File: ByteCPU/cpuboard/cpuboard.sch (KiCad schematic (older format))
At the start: 4 parts, among them J1 Conn_01x06, J2 Conn_01x20, J3 Conn_01x08

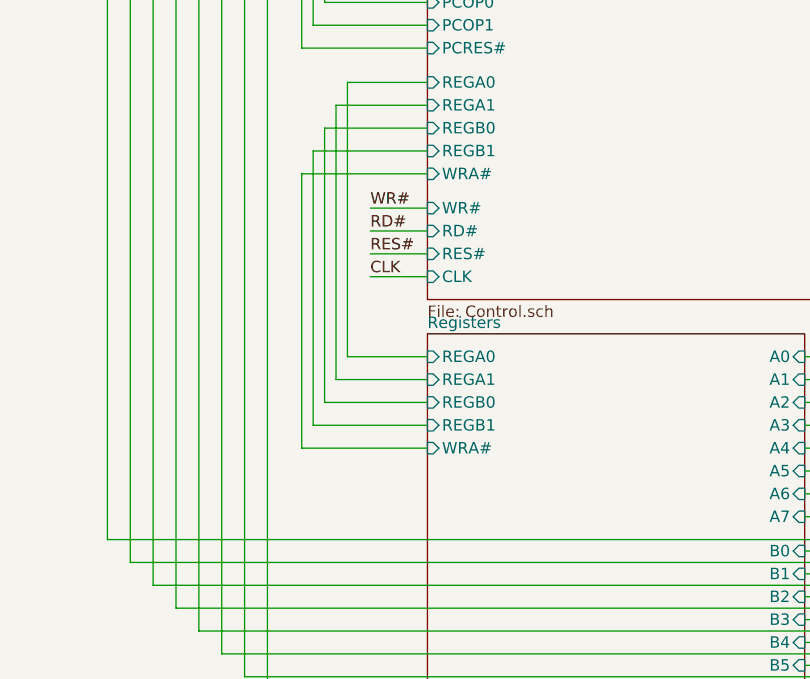
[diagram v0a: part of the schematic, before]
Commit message: Fix mistake in SELPC signal generation. More docu.
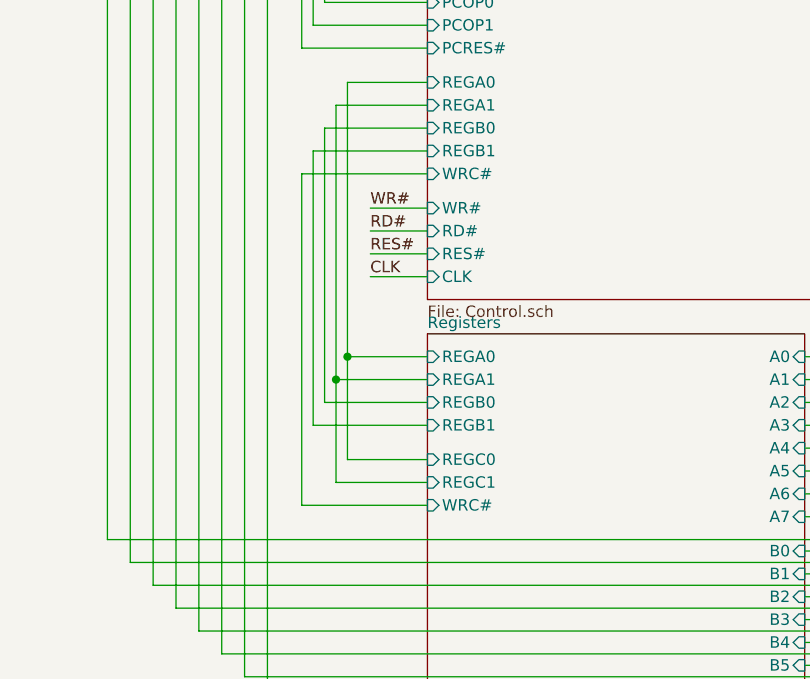
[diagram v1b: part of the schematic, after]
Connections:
- wire segments 221 -> 225
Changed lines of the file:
@@
 F0 "Registers" 50
 F1 "registers.sch" 50
-F2 "WRA#" I L 2000 5500 50
-F3 "CLK" I L 2000 7500 50
-F4 "C0" I R 3650 6800 50
-F5 "C1" I R 3650 6900 50
-F6 "C2" I R 3650 7000 50
-F7 "C3" I R 3650 7100 50
-F8 "C4" I R 3650 7200 50
-F9 "C5" I R 3650 7300 50
-F10 "C6" I R 3650 7400 50
-F11 "C7" I R 3650 7500 50
-F12 "REGB0" I L 2000 5300 50
-F13 "REGB1" I L 2000 5400 50
-F14 "REGA0" I L 2000 5100 50
-F15 "REGA1" I L 2000 5200 50
-F16 "A0" I R 3650 5100 50
-F17 "A1" I R 3650 5200 50
-F18 "A2" I R 3650 5300 50
-F19 "A3" I R 3650 5400 50
-F20 "A4" I R 3650 5500 50
-F21 "A5" I R 3650 5600 50
-F22 "A6" I R 3650 5700 50
-F23 "A7" I R 3650 5800 50
-F24 "B0" I R 3650 5950 50
-F25 "B1" I R 3650 6050 50
-F26 "B2" I R 3650 6150 50
-F27 "B3" I R 3650 6250 50
-F28 "B4" I R 3650 6350 50
-F29 "B5" I R 3650 6450 50
-F30 "B6" I R 3650 6550 50
-F31 "B7" I R 3650 6650 50
+F2 "CLK" I L 2000 7500 50
+F3 "C0" I R 3650 6800 50
+F4 "C1" I R 3650 6900 50
+F5 "C2" I R 3650 7000 50
+F6 "C3" I R 3650 7100 50
+F7 "C4" I R 3650 7200 50
+F8 "C5" I R 3650 7300 50
+F9 "C6" I R 3650 7400 50
+F10 "C7" I R 3650 7500 50
+F11 "REGB0" I L 2000 5300 50
+F12 "REGB1" I L 2000 5400 50
+F13 "REGA0" I L 2000 5100 50
+F14 "REGA1" I L 2000 5200 50
+F15 "A0" I R 3650 5100 50
+F16 "A1" I R 3650 5200 50
+F17 "A2" I R 3650 5300 50
+F18 "A3" I R 3650 5400 50
+F19 "A4" I R 3650 5500 50
+F20 "A5" I R 3650 5600 50
+F21 "A6" I R 3650 5700 50
+F22 "A7" I R 3650 5800 50
+F23 "B0" I R 3650 5950 50
+F24 "B1" I R 3650 6050 50
+F25 "B2" I R 3650 6150 50
+F26 "B3" I R 3650 6250 50
+F27 "B4" I R 3650 6350 50
+F28 "B5" I R 3650 6450 50
+F29 "B6" I R 3650 6550 50
+F30 "B7" I R 3650 6650 50
+F31 "WRC#" I L 2000 5750 50
+F32 "REGC0" I L 2000 5550 50
+F33 "REGC1" I L 2000 5650 50
 $EndSheet
 $Sheet
@@
 F19 "WRDP#" I L 2000 3450 50
 F20 "SELALU#" I R 5800 4250 50
-F21 "WRA#" I L 2000 4300 50
-F22 "ISTRUE" I R 5800 4350 50
-F23 "REGA0" I L 2000 3900 50
-F24 "REGA1" I L 2000 4000 50
-F25 "REGB0" I L 2000 4100 50
-F26 "REGB1" I L 2000 4200 50
-F27 "OP1" I R 5800 4500 50
-F28 "OP2" I R 5800 4600 50
-F29 "OP3" I R 5800 4700 50
+F21 "ISTRUE" I R 5800 4350 50
+F22 "REGA0" I L 2000 3900 50
+F23 "REGA1" I L 2000 4000 50
+F24 "REGB0" I L 2000 4100 50
+F25 "REGB1" I L 2000 4200 50
+F26 "OP1" I R 5800 4500 50
+F27 "OP2" I R 5800 4600 50
+F28 "OP3" I R 5800 4700 50
+F29 "WRC#" I L 2000 4300 50
 $EndSheet
 Text Label 9150 6350 3    50   ~ 0
@@
 	1650 3900 1650 5100
 Wire Wire Line
-	1650 5100 2000 5100
-Wire Wire Line
 	2000 5200 1600 5200
 Wire Wire Line
@@
 Wire Wire Line
 	2000 4300 1450 4300
-Wire Wire Line
-	1450 4300 1450 5500
-Wire Wire Line
-	1450 5500 2000 5500
 Text Label 1750 4750 0    50   ~ 0
 CLK
@@
 Text Notes 10250 5200 0    50   ~ 0
 Add a 100nF ceramic \ncapacitor to every IC.
+Wire Wire Line
+	1450 5750 2000 5750
+Wire Wire Line
+	1450 4300 1450 5750
+Wire Wire Line
+	1650 5100 2000 5100
+Wire Wire Line
+	1650 5100 1650 5550
+Wire Wire Line
+	1650 5550 2000 5550
+Connection ~ 1650 5100
+Wire Wire Line
+	1600 5200 1600 5650
+Wire Wire Line
+	1600 5650 2000 5650
+Connection ~ 1600 5200
 $EndSCHEMATC

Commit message: Modifications to fit the wiring to the physical layout of the 7400 logic. Bugfix: RD line was active during JMP instruction.
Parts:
- removed J2: Conn_01x20, symbol Connector_Generic:Conn_01x20
- added J2: Conn_01x18, symbol Connector_Generic:Conn_01x18
- added U1: 7400, symbol 74xx:7400
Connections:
- wire segments 225 -> 246
- no-connect marks 0 -> 1

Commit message: Rework control logic to allow and additional IO instruction
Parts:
- removed J1: Conn_01x06, symbol Connector_Generic:Conn_01x06
- removed J2: Conn_01x18, symbol Connector_Generic:Conn_01x18
- removed unit 3 of U1
- removed unit 4 of U1
- added J1: Conn_01x07, symbol Connector_Generic:Conn_01x07
- added J2: Conn_01x17, symbol Connector_Generic:Conn_01x17
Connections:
- net labels added: IO#
- wire segments 246 -> 237
- no-connect marks 1 -> 0
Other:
- moved on the sheet: U1B
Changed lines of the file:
@@
 F40 "COUNT" I L 2000 2750 50
-$EndSheet
-$Sheet
-S 2000 3200 3800 1650
-U 6088908D
-F0 "Control" 50
-F1 "Control.sch" 50
-F2 "D0" I R 5800 3300 50
-F3 "D1" I R 5800 3400 50
-F4 "D2" I R 5800 3500 50
-F5 "D3" I R 5800 3600 50
-F6 "D4" I R 5800 3700 50
-F7 "D5" I R 5800 3800 50
-F8 "D6" I R 5800 3900 50
-F9 "D7" I R 5800 4000 50
-F10 "CLK" I L 2000 4750 50
-F11 "RES#" I L 2000 4650 50
-F12 "WR#" I L 2000 4450 50
-F13 "RD#" I L 2000 4550 50
-F14 "PCRES#" I L 2000 3800 50
-F15 "SELPC" I L 2000 3300 50
-F16 "OEA#" I R 5800 4150 50
-F17 "WRDP#" I L 2000 3400 50
-F18 "SELALU#" I R 5800 4250 50
-F19 "ISTRUE" I R 5800 4350 50
-F20 "REGA0" I L 2000 3900 50
-F21 "REGA1" I L 2000 4000 50
-F22 "REGB0" I L 2000 4100 50
-F23 "REGB1" I L 2000 4200 50
-F24 "OP1" I R 5800 4500 50
-F25 "OP2" I R 5800 4600 50
-F26 "OP3" I R 5800 4700 50
-F27 "WRC#" I L 2000 4300 50
-F28 "COUNT" I L 2000 3700 50
-F29 "LOADLOW#" I L 2000 3600 50
-F30 "LOADHIGH#" I L 2000 3500 50
 $EndSheet
 Text Label 9650 6350 3    50   ~ 0
@@
 	3800 6650 4200 6650
 $Comp
-L Connector_Generic:Conn_01x06 J1
-U 1 1 60D740B8
-P 950 650
-F 0 "J1" V 916 930 50  0000 L CNN
-F 1 "Conn_01x06" V 1050 400 50  0000 L CNN
-F 2 "" H 950 650 50  0001 C CNN
-F 3 "~" H 950 650 50  0001 C CNN
-	1    950  650
-	0    1    -1   0
-$EndComp
-$Comp
 L power:GND #PWR0145
 U 1 1 60D7414A
@@
 Wire Wire Line
 	2000 4300 1450 4300
-Text Label 1750 4750 0    50   ~ 0
+Text Label 1750 4800 0    50   ~ 0
 CLK
-Text Label 1750 4650 0    50   ~ 0
+Text Label 1750 4700 0    50   ~ 0
 RES#
-Text Label 1750 4550 0    50   ~ 0
+Text Label 1750 4600 0    50   ~ 0
 RD#
-Text Label 1750 4450 0    50   ~ 0
+Text Label 1750 4500 0    50   ~ 0
 WR#
 Wire Wire Line
-	1750 4450 2000 4450
-Wire Wire Line
-	1750 4550 2000 4550
-Wire Wire Line
-	1750 4650 2000 4650
-Wire Wire Line
-	1750 4750 2000 4750
+	1750 4500 2000 4500
+Wire Wire Line
+	1750 4600 2000 4600
+Wire Wire Line
+	1750 4700 2000 4700
+Wire Wire Line
+	1750 4800 2000 4800
 Wire Wire Line
 	5800 4150 6100 4150
@@
 P 1150 1300
 F 0 "U1" H 1350 1550 50  0000 C CNN
-F 1 "7400" H 1350 1450 50  0000 C CNN
+F 1 "7400" H 1400 1450 50  0000 C CNN
 F 2 "" H 1150 1300 50  0001 C CNN
 F 3 "http://www.ti.com/lit/gpn/sn7400" H 1150 1300 50  0001 C CNN
@@
 L 74xx:7400 U1
 U 2 1 5FAC56A9
-P 6500 850
-F 0 "U1" H 6650 1150 50  0000 C CNN
-F 1 "7400" H 6650 1050 50  0000 C CNN
-F 2 "" H 6500 850 50  0001 C CNN
-F 3 "http://www.ti.com/lit/gpn/sn7400" H 6500 850 50  0001 C CNN
-	2    6500 850
-	1    0    0    -1
-$EndComp
-$Comp
-L 74xx:7400 U1
-U 3 1 5FAC56F1
-P 10650 2550
-F 0 "U1" H 10650 2875 50  0000 C CNN
-F 1 "7400" H 10650 2784 50  0000 C CNN
-F 2 "" H 10650 2550 50  0001 C CNN
-F 3 "http://www.ti.com/lit/gpn/sn7400" H 10650 2550 50  0001 C CNN
-	3    10650 2550
-	1    0    0    -1
-$EndComp
-$Comp
-L 74xx:7400 U1
-U 4 1 5FAC573E
-P 6500 1250
-F 0 "U1" H 6700 1500 50  0000 C CNN
-F 1 "7400" H 6700 1400 50  0000 C CNN
-F 2 "" H 6500 1250 50  0001 C CNN
-F 3 "http://www.ti.com/lit/gpn/sn7400" H 6500 1250 50  0001 C CNN
-	4    6500 1250
+P 6500 1150
+F 0 "U1" H 6650 1450 50  0000 C CNN
+F 1 "7400" H 6650 1350 50  0000 C CNN
+F 2 "" H 6500 1150 50  0001 C CNN
+F 3 "http://www.ti.com/lit/gpn/sn7400" H 6500 1150 50  0001 C CNN
+	2    6500 1150
 	1    0    0    -1
 $EndComp
@@
 	5800 1450 5900 1450
 Wire Wire Line
-	5800 1550 6100 1550
-Wire Wire Line
 	5800 1650 7400 1650
 Wire Wire Line
@@
 Wire Wire Line
 	5800 2950 8700 2950
-$Comp
-L Connector_Generic:Conn_01x18 J2
-U 1 1 5FED44A1
-P 7900 650
-F 0 "J2" V 8117 596 50  0000 C CNN
-F 1 "Conn_01x18" V 8026 596 50  0000 C CNN
-F 2 "" H 7900 650 50  0001 C CNN
-F 3 "~" H 7900 650 50  0001 C CNN
-	1    7900 650
-	0    1    -1   0
-$EndComp
-Wire Wire Line
-	6800 850  7000 850
-Wire Wire Line
-	6800 1250 7100 1250
-Wire Wire Line
-	7100 1250 7100 850
-Wire Wire Line
-	6000 1450 6000 1150
-Connection ~ 6000 1450
-Wire Wire Line
-	6000 1450 7200 1450
-Wire Wire Line
-	6150 750  6150 850
-Wire Wire Line
-	6150 950  6200 950
-Wire Wire Line
-	6150 750  6200 750
-Wire Wire Line
-	6000 1150 6200 1150
-Wire Wire Line
-	6100 1550 6100 1350
-Wire Wire Line
-	6100 1350 6200 1350
-Connection ~ 6100 1550
-Wire Wire Line
-	6100 1550 7300 1550
-Connection ~ 6150 850
-Wire Wire Line
-	6150 850  6150 950
-Wire Wire Line
-	5900 1450 5900 850
+Wire Wire Line
+	5900 1450 5900 1150
 Connection ~ 5900 1450
-Wire Wire Line
-	5900 1450 6000 1450
-Wire Wire Line
-	5900 850  6150 850
 $Comp
 L power:GND #PWR?
@@
 Wire Wire Line
 	10600 1850 10600 1800
-$Comp
-L power:GND #PWR?
-U 1 1 5FFA0844
-P 10300 2700
-F 0 "#PWR?" H 10300 2450 50  0001 C CNN
-F 1 "GND" H 10305 2527 50  0000 C CNN
-F 2 "" H 10300 2700 50  0001 C CNN
-F 3 "" H 10300 2700 50  0001 C CNN
-	1    10300 2700
-	1    0    0    -1
-$EndComp
-Wire Wire Line
-	10300 2700 10300 2650
-Wire Wire Line
-	10300 2650 10350 2650
-Wire Wire Line
-	10300 2650 10300 2450
-Wire Wire Line
-	10300 2450 10350 2450
-Connection ~ 10300 2650
-NoConn ~ 10950 2550
+$Sheet
+S 2000 3200 3800 1650
+U 6088908D
+F0 "Control" 50
+F1 "Control.sch" 50
+F2 "D0" I R 5800 3300 50
+F3 "D1" I R 5800 3400 50
+F4 "D2" I R 5800 3500 50
+F5 "D3" I R 5800 3600 50
+F6 "D4" I R 5800 3700 50
+F7 "D5" I R 5800 3800 50
+F8 "D6" I R 5800 3900 50
+F9 "D7" I R 5800 4000 50
+F10 "CLK" I L 2000 4800 50
+F11 "RES#" I L 2000 4700 50
+F12 "WR#" I L 2000 4500 50
+F13 "RD#" I L 2000 4600 50
+F14 "PCRES#" I L 2000 3800 50
+F15 "SELPC" I L 2000 3300 50
+F16 "OEA#" I R 5800 4150 50
+F17 "WRDP#" I L 2000 3400 50
+F18 "SELALU#" I R 5800 4250 50
+F19 "ISTRUE" I R 5800 4350 50
+F20 "REGA0" I L 2000 3900 50
+F21 "REGA1" I L 2000 4000 50
+F22 "REGB0" I L 2000 4100 50
+F23 "REGB1" I L 2000 4200 50
+F24 "OP1" I R 5800 4600 50
+F25 "OP2" I R 5800 4700 50
+F26 "WRC#" I L 2000 4300 50
+F27 "COUNT" I L 2000 3700 50
+F28 "LOADLOW#" I L 2000 3600 50
+F29 "LOADHIGH#" I L 2000 3500 50
+F30 "IO#" I L 2000 4400 50
+F31 "OP0" I R 5800 4500 50
+$EndSheet
+Wire Wire Line
+	5900 1450 7200 1450
+Wire Wire Line
+	5800 1550 7300 1550
+$Comp
+L Connector_Generic:Conn_01x17 J2
+U 1 1 5FB28B42
+P 7900 650
+F 0 "J2" V 7900 1550 50  0000 C CNN
+F 1 "Conn_01x17" V 8000 650 50  0000 C CNN
+F 2 "" H 7900 650 50  0001 C CNN
+F 3 "~" H 7900 650 50  0001 C CNN
+	1    7900 650
+	0    1    -1   0
+$EndComp
+Wire Wire Line
+	6200 1050 6150 1050
+Wire Wire Line
+	6150 1050 6150 1150
+Wire Wire Line
+	6150 1250 6200 1250
+Wire Wire Line
+	6150 1150 5900 1150
+Connection ~ 6150 1150
+Wire Wire Line
+	6150 1150 6150 1250
+Wire Wire Line
+	6800 1150 7100 1150
+Wire Wire Line
+	7100 1150 7100 850
+$Comp
+L Connector_Generic:Conn_01x07 J1
+U 1 1 5FB65E27
+P 950 650
+F 0 "J1" V 916 1030 50  0000 L CNN
+F 1 "Conn_01x07" V 1050 450 50  0000 L CNN
+F 2 "" H 950 650 50  0001 C CNN
+F 3 "~" H 950 650 50  0001 C CNN
+	1    950  650
+	0    1    -1   0
+$EndComp
+Text Label 1250 1050 1    50   ~ 0
+IO#
+Wire Wire Line
+	1250 1050 1250 850
+Text Label 1750 4400 0    50   ~ 0
+IO#
+Wire Wire Line
+	1750 4400 2000 4400
 $EndSCHEMATC

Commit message: Rework all opcodes to speed up the decoding stage by 10 ns
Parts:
- removed J1: Conn_01x07, symbol Connector_Generic:Conn_01x07
- added J1: Conn_01x06, symbol Connector_Generic:Conn_01x06
- added unit 3 of U1
- added unit 4 of U1
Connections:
- net labels removed: IO#
- wire segments 237 -> 243
- no-connect marks 0 -> 2
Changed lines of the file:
@@
 F38 "D6" I R 5800 6150 50
 F39 "D7" I R 5800 6250 50
-F40 "SELALU#" I R 5800 5200 50
+F40 "SELMEM" I R 5800 5200 50
 $EndSheet
 $Sheet
@@
 F34 "D6" I L 2000 1250 50
 F35 "D7" I L 2000 1350 50
-F36 "SELPC" I L 2000 2350 50
-F37 "PCRES#" I L 2000 2850 50
-F38 "LOADHIGH#" I L 2000 2550 50
-F39 "LOADLOW#" I L 2000 2650 50
-F40 "COUNT" I L 2000 2750 50
+F36 "PCRES#" I L 2000 2850 50
+F37 "LOADHIGH#" I L 2000 2550 50
+F38 "LOADLOW#" I L 2000 2650 50
+F39 "COUNT" I L 2000 2750 50
+F40 "SELADR" I L 2000 2350 50
 $EndSheet
 Text Label 9650 6350 3    50   ~ 0
@@
 Connection ~ 5900 1450
 $Comp
-L power:GND #PWR?
+L power:GND #PWR0144
 U 1 1 5FF81CCD
 P 10600 1850
-F 0 "#PWR?" H 10600 1600 50  0001 C CNN
+F 0 "#PWR0144" H 10600 1600 50  0001 C CNN
 F 1 "GND" H 10605 1677 50  0000 C CNN
 F 2 "" H 10600 1850 50  0001 C CNN
@@
 $EndComp
 $Comp
-L power:+5V #PWR?
+L power:+5V #PWR0180
 U 1 1 5FF81D08
 P 10600 750
-F 0 "#PWR?" H 10600 600 50  0001 C CNN
+F 0 "#PWR0180" H 10600 600 50  0001 C CNN
 F 1 "+5V" H 10615 923 50  0000 C CNN
 F 2 "" H 10600 750 50  0001 C CNN
@@
 F13 "RD#" I L 2000 4600 50
 F14 "PCRES#" I L 2000 3800 50
-F15 "SELPC" I L 2000 3300 50
-F16 "OEA#" I R 5800 4150 50
-F17 "WRDP#" I L 2000 3400 50
-F18 "SELALU#" I R 5800 4250 50
-F19 "ISTRUE" I R 5800 4350 50
-F20 "REGA0" I L 2000 3900 50
-F21 "REGA1" I L 2000 4000 50
-F22 "REGB0" I L 2000 4100 50
-F23 "REGB1" I L 2000 4200 50
-F24 "OP1" I R 5800 4600 50
-F25 "OP2" I R 5800 4700 50
-F26 "WRC#" I L 2000 4300 50
-F27 "COUNT" I L 2000 3700 50
-F28 "LOADLOW#" I L 2000 3600 50
-F29 "LOADHIGH#" I L 2000 3500 50
-F30 "IO#" I L 2000 4400 50
-F31 "OP0" I R 5800 4500 50
+F15 "OEA#" I R 5800 4150 50
+F16 "WRDP#" I L 2000 3400 50
+F17 "ISTRUE" I R 5800 4350 50
+F18 "REGA0" I L 2000 3900 50
+F19 "REGA1" I L 2000 4000 50
+F20 "REGB0" I L 2000 4100 50
+F21 "REGB1" I L 2000 4200 50
+F22 "OP1" I R 5800 4600 50
+F23 "OP2" I R 5800 4700 50
+F24 "WRC#" I L 2000 4300 50
+F25 "COUNT" I L 2000 3700 50
+F26 "LOADLOW#" I L 2000 3600 50
+F27 "LOADHIGH#" I L 2000 3500 50
+F28 "OP0" I R 5800 4500 50
+F29 "SELMEM" I R 5800 4250 50
+F30 "SELADR" I L 2000 3300 50
 $EndSheet
 Wire Wire Line
@@
 	7100 1150 7100 850
 $Comp
-L Connector_Generic:Conn_01x07 J1
-U 1 1 5FB65E27
+L 74xx:7400 U1
+U 3 1 5FECED65
+P 10600 2750
+AR Path="/5FECED65" Ref="U1"  Part="3"
+AR Path="/60888F9A/5FECED65" Ref="U?"  Part="3"
+F 0 "U1" H 10600 3075 50  0000 C CNN
+F 1 "7400" H 10600 2984 50  0000 C CNN
+F 2 "" H 10600 2750 50  0001 C CNN
+F 3 "http://www.ti.com/lit/gpn/sn7400" H 10600 2750 50  0001 C CNN
+	3    10600 2750
+	1    0    0    -1
+$EndComp
+$Comp
+L 74xx:7400 U1
+U 4 1 5FECED6C
+P 10600 3300
+AR Path="/5FECED6C" Ref="U1"  Part="4"
+AR Path="/60888F9A/5FECED6C" Ref="U?"  Part="4"
+F 0 "U1" H 10800 3550 50  0000 C CNN
+F 1 "7400" H 10800 3450 50  0000 C CNN
+F 2 "" H 10600 3300 50  0001 C CNN
+F 3 "http://www.ti.com/lit/gpn/sn7400" H 10600 3300 50  0001 C CNN
+	4    10600 3300
+	1    0    0    -1
+$EndComp
+NoConn ~ 10900 2750
+NoConn ~ 10900 3300
+$Comp
+L power:GND #PWR0181
+U 1 1 5FEFA9A6
+P 10250 3500
+F 0 "#PWR0181" H 10250 3250 50  0001 C CNN
+F 1 "GND" H 10255 3327 50  0000 C CNN
+F 2 "" H 10250 3500 50  0001 C CNN
+F 3 "" H 10250 3500 50  0001 C CNN
+	1    10250 3500
+	1    0    0    -1
+$EndComp
+Wire Wire Line
+	10250 3500 10250 3400
+Wire Wire Line
+	10250 3400 10300 3400
+Wire Wire Line
+	10250 3400 10250 3200
+Wire Wire Line
+	10250 3200 10300 3200
+Connection ~ 10250 3400
+Wire Wire Line
+	10250 3200 10250 2850
+Wire Wire Line
+	10250 2850 10300 2850
+Connection ~ 10250 3200
+Wire Wire Line
+	10250 2850 10250 2650
+Wire Wire Line
+	10250 2650 10300 2650
+Connection ~ 10250 2850
+$Comp
+L Connector_Generic:Conn_01x06 J1
+U 1 1 5FF37057
 P 950 650
-F 0 "J1" V 916 1030 50  0000 L CNN
-F 1 "Conn_01x07" V 1050 450 50  0000 L CNN
+F 0 "J1" V 916 930 50  0000 L CNN
+F 1 "Conn_01x06" V 825 930 50  0000 L CNN
 F 2 "" H 950 650 50  0001 C CNN
 F 3 "~" H 950 650 50  0001 C CNN
@@
 	0    1    -1   0
 $EndComp
-Text Label 1250 1050 1    50   ~ 0
-IO#
-Wire Wire Line
-	1250 1050 1250 850
-Text Label 1750 4400 0    50   ~ 0
-IO#
-Wire Wire Line
-	1750 4400 2000 4400
+Connection ~ 3550 2050
 $EndSCHEMATC
